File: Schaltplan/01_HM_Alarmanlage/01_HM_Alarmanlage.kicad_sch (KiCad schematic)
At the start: 8 parts, among them Q1 IRLB8721PBF

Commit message: add: Schaltplan Fertig
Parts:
- removed D2: LED, symbol Device:LED
- removed R4: 8,2, symbol Device:R
- added BZ1: Buzzer, symbol Device:Buzzer
- added J1: Ultraschallsensor, symbol Connector_Generic:Conn_01x04
- added J2: I2C Display, symbol Connector_Generic:Conn_01x04
- added J5: IRL_Sensor, symbol Connector_Generic:Conn_01x04
- added J6: Powerbank, symbol Connector_Generic:Conn_01x02
- added LS1, LS2: Speaker, symbol Device:Speaker
- added Q2, Q3: IRLB8721PBF, Package_TO_SOT_THT:TO-220-3_Vertical, symbol Transistor_FET:IRLB8721PBF
- added R10, R6, R8, R9: 10k, symbol Device:R
- added R5, R7: 100, symbol Device:R
- added SW1: Taste, symbol Switch:SW_Push
- added SW2: Hauptschalter, symbol Switch:SW_SPST
- added U1: PAM8406D, Package_SO:SOIC-16_3.9x9.9mm_P1.27mm, symbol Amplifier_Audio:PAM8406D
- A1: value Arduino_Nano_v3.x -> Arduino_Nano_33_IoT
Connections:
- net +5V: now also BZ1.1 (+), J5.3 (Pin_3), R10.1, R9.1, SW2.2 (B), U1.13 (PVDDR), U1.4 (PVDDL), U1.6 (VDD)
- net GND: now also J1.4 (Pin_4), J2.4 (Pin_4), J5.4 (Pin_4), J6.2 (Pin_2), Q2.3 (S), Q3.3 (S), R6.2, R8.2, SW1.2, U1.11 (GND), U1.15 (PGNDR), U1.2 (PGNDL)
- net at A1.11 (D8): now also SW1.1; no longer R2.1
- net O_Buzz: now reaches A1.10 (D7)
- net O_Buzz: now also R5.1
- net O_SpeakerL: now reaches A1.19 (A0)
- net O_SpeakerL: now also U1.7 (INL)
- net aSig_USS: now reaches A1.20 (A1)
- net aSig_USS: now also J1.1 (Pin_1)
- net SDA: now reaches A1.23 (A4)
- net SDA: now also J2.2 (Pin_2), R9.2
- net SCL: now reaches A1.24 (A5)
- net SCL: now also J2.1 (Pin_1), R10.2
- net IN_Taste: now reaches A1.7 (D4)
- net Sig_IRL: now reaches A1.8 (D5)
- net Sig_IRL: now also J5.1 (Pin_1)
- net O_LED: now reaches A1.9 (D6)
- net O_LED: now also R2.1
- new net: Q3.1 (G), R7.2, R8.1
- new net: Q2.1 (G), R5.2, R6.1
- new net: J6.1 (Pin_1), SW2.1 (A)
- new net: BZ1.2 (-), Q2.2 (D)
- new net: LS2.1, U1.14 (-OUT_R)
- new net: LS2.2, U1.16 (+OUT_R)
- new net: LS1.1, U1.1 (+OUT_L)
- new net: LS1.2, U1.3 (-OUT_L)
- new net +3.3V: J1.3 (Pin_3), J2.3 (Pin_3)
- new net Mode: U1.9 (MODE)
- new net Mute: U1.5 (~{MUTE})
- new net O_SpeakerR: U1.10 (INR)
- new net SHND: U1.12 (~{SHND})
- no-connect marks 0 -> 2
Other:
- note added: "Ausgang Akustisch"
- note added: "Ausgang Optisch"
- note added: "Eingang Elektrsich"
- note added: "Eingang ext. Sensorisch"
- note added: "MCUisch"
- note removed: "MCU PWM Pin"
- note removed: "optional"
- title: (none) -> Alarmanlage
- moved on the sheet: A1, D1, Q1, R1, R2, R3

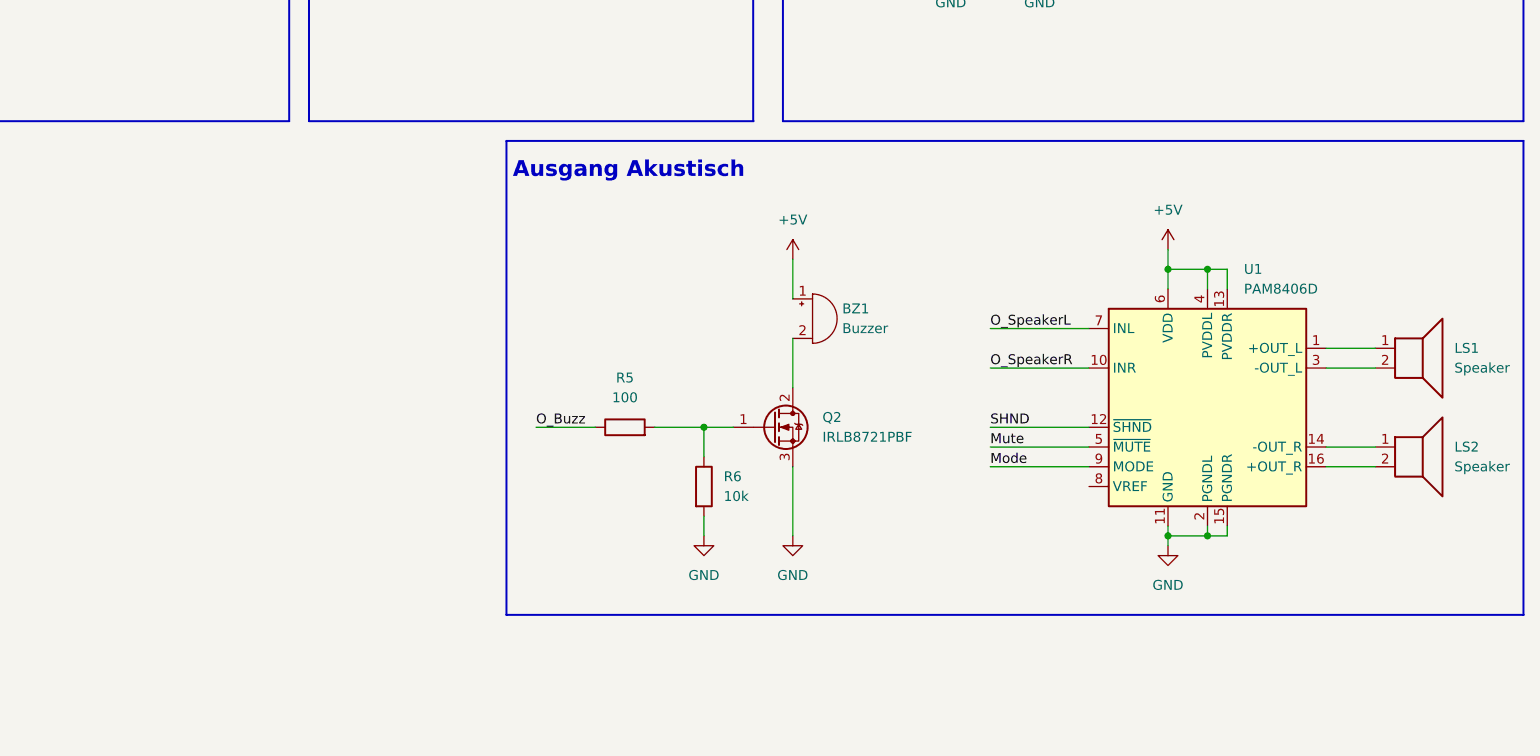
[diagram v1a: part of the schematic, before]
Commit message: add: Lautsprecher 14Pin Connector hinzugefügt
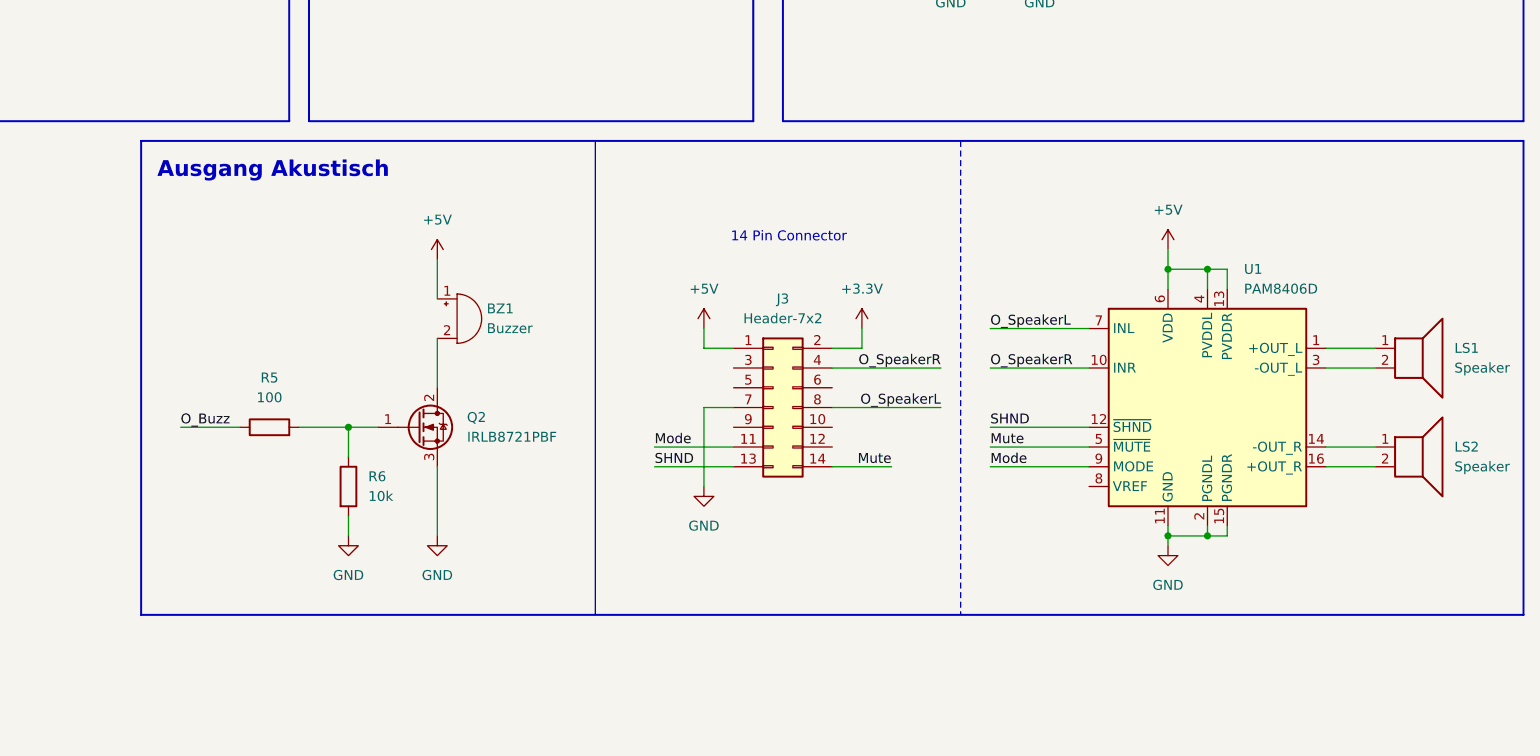
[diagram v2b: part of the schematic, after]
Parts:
- added J3: Header-7x2, symbol Connector_Generic:Conn_02x07_Odd_Even
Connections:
- net +3.3V: now also J3.2 (Pin_2)
- net +5V: now also J3.1 (Pin_1)
- net GND: now also J3.7 (Pin_7)
- net Mode: now also J3.11 (Pin_11)
- net Mute: now also J3.14 (Pin_14)
- net O_SpeakerL: now also J3.8 (Pin_8)
- net O_SpeakerR: now also J3.4 (Pin_4)
- net SHND: now also J3.13 (Pin_13)
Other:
- note added: "14 Pin Connector"
- moved on the sheet: BZ1, Q2, R5, R6

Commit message: add: Adapter Platine für den Anschluss von LED & Buzzer. add: Bilder von AdapterPlatine & Pinout Lautsprecher im Schaltplan vorläufig ergänzt
TODOs:
-Bilder skalieren, zuschneiden und beschriften
-Schaltplan schön machen
-Verdrahtung korrigieren
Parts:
- added BZ2: Buzzer, symbol Device:Buzzer
- added D2: LED, symbol Device:LED
- added J4, J7: Conn_01x04, symbol Connector_Generic:Conn_01x04
- added J8: Conn_01x03, symbol Connector_Generic:Conn_01x03
- added J9: Conn_01x02, symbol Connector_Generic:Conn_01x02
- added Q4, Q5: IRLB8721PBF, Package_TO_SOT_THT:TO-220-3_Vertical, symbol Transistor_FET:IRLB8721PBF
- added R11, R14: 10k, symbol Device:R
- added R12: 8,2, symbol Device:R
- added R13, R4: 100, symbol Device:R
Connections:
- net +5V: now also J7.2 (Pin_2), J7.3 (Pin_3), J9.1 (Pin_1), J9.2 (Pin_2)
- net GND: now also J8.1 (Pin_1), Q4.3 (S), Q5.3 (S), R11.2, R14.2
- net O_Buzz: now also J8.3 (Pin_3), R13.1
- net O_LED: now also J8.2 (Pin_2), R4.1
- new net: BZ2.1 (+), J4.3 (Pin_3)
- new net: BZ2.2 (-), J4.4 (Pin_4)
- new net: Q4.2 (D), R12.1
- new net: J7.1 (Pin_1), R12.2
- new net: Q5.1 (G), R13.2, R14.1
- new net: D2.1 (K), J4.1 (Pin_1)
- new net: D2.2 (A), J4.2 (Pin_2)
- new net: Q4.1 (G), R11.1, R4.2
- new net: J7.4 (Pin_4), Q5.2 (D)
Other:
- note added: "4pol. Connector: LED + Buzzer 1: geschaltete Masse Buzzer 2/3: +5V (dauerhaft) 4: geschaltete Masse LED"
- note added: "Adapter Platine"
